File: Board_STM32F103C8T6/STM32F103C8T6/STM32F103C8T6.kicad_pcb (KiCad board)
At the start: 4 copper layers, 96 x 96 mm, 113 parts, among them J301 BOOT, J401 BATTERY, J402 I2C, J403 H2O, J404 USB_B_Micro, J405 SWD, J406 USART1, J407 CIRCUIT_SENSOR, J408 BLUETOOTH, J409 RPM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

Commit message: updated layout
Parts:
- C702: value 250n -> 220n
- R703: value 4,7K -> 4k7
- U201: value LD1117S33TR_SOT223 -> LD1117S33TR

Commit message: Changed Crystals
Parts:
- C201, C302, C303, C304, C305, C308, C401, C502, C503, C504, C602, C802, C803, C804: value 100n -> 0.1uF
- C202, C501, C601, C701, C703, C801: value 10u -> 10uF
- C301: value 4u7 -> 4.7uF
- C306: value 1u -> 1uF
- C307, C805: value 10n -> 0.01uF
- C309, C311: value 12p -> 24pF
- C310, C312: value 6.8p -> 13pF
- C402, C403: value 47p -> 47pF
- C505: value 2n2 -> 2200pF
- C702: value 220n -> 0.1uF
- L301: value 39n -> 39nH
- L801: value 100n -> 100nH
- R201, R311, R319, R603: value 1k5 -> 1.5kΩ
- R301, R302: value 2k2 -> 2.2kΩ
- R303, R304, R306, R308, R309, R310, R313, R314: value 100k -> 100kΩ
- R305: value 1k5 -> 787Ω
- R307: value 7.5k -> 36kΩ
- R312, R705: value 100 -> 100kΩ
- R315, R316, R318, R320: value 10k -> 10kΩ
- R317: value 4k7 -> 4.7kΩ
- R401, R402: value 22 -> 22kΩ
- R601, R602: value 1k -> 1kΩ
- R701, R702, R704, R706: value 10K -> 10kΩ
- R703: value 4k7 -> 10kΩ
- R801, R802: value 0 -> 0kΩ
- R803: value 10 -> 10kΩ
- Y301: value 8Mhz -> 8MHz; footprint Crystal:Crystal_SMD_5032-2Pin_5.0x3.2mm_HandSoldering -> Crystal:Crystal_SMD_HC49-SD_HandSoldering
- Y302: value 32.768KHZ -> 32.768KHz; footprint Crystal:Crystal_SMD_3215-2Pin_3.2x1.5mm -> Crystal:Crystal_SMD_Abracon_ABS25-4Pin_8.0x3.8mm
- moved Y301 4.27 mm to (108.5, 80.0)
- moved C310 4.19 mm to (113.0, 57.0), turned to 90 degrees
- moved R706 3.76 mm to (124.0, 87.0), turned to 90 degrees
- moved C309 3.10 mm to (113.0, 71.0), turned to 90 degrees
- moved C311 2.97 mm to (113.0, 82.5), turned to 270 degrees
- moved Y302 2.69 mm to (108.5, 61.0), turned to 0 degrees
- moved R307 1.80 mm to (113.0, 66.5)
- turned C312 to 180 degrees
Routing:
- net LSE_IN: track 19.3 -> 27.6 mm
- net USART2_RX: track 94.2 -> 102.4 mm
- net USART2_TX: track 97.1 -> 104.5 mm
- net GND: track 63.2 -> 69.8 mm, vias 84 -> 88
- net +5V: track 72.3 -> 65.9 mm
- net LED_STATUS: track 35.6 -> 41.7 mm
- net +3V3: track 152.2 -> 147.1 mm, vias 40 -> 41
- net H2O_NTC+: track 54.9 -> 49.9 mm, vias 1 -> 0
- net Net-(C312-Pad1): track 4.89 -> 7.95 mm
- net Net-(C311-Pad1): track 11.8 -> 9.49 mm
- net BOOT0: track 67.4 -> 69.6 mm
- net LSE_OUT: track 12.4 -> 10.8 mm
- net RPM_SENSOR: track 16.1 -> 15.0 mm
- net HSE_IN: track 14.2 -> 13.4 mm

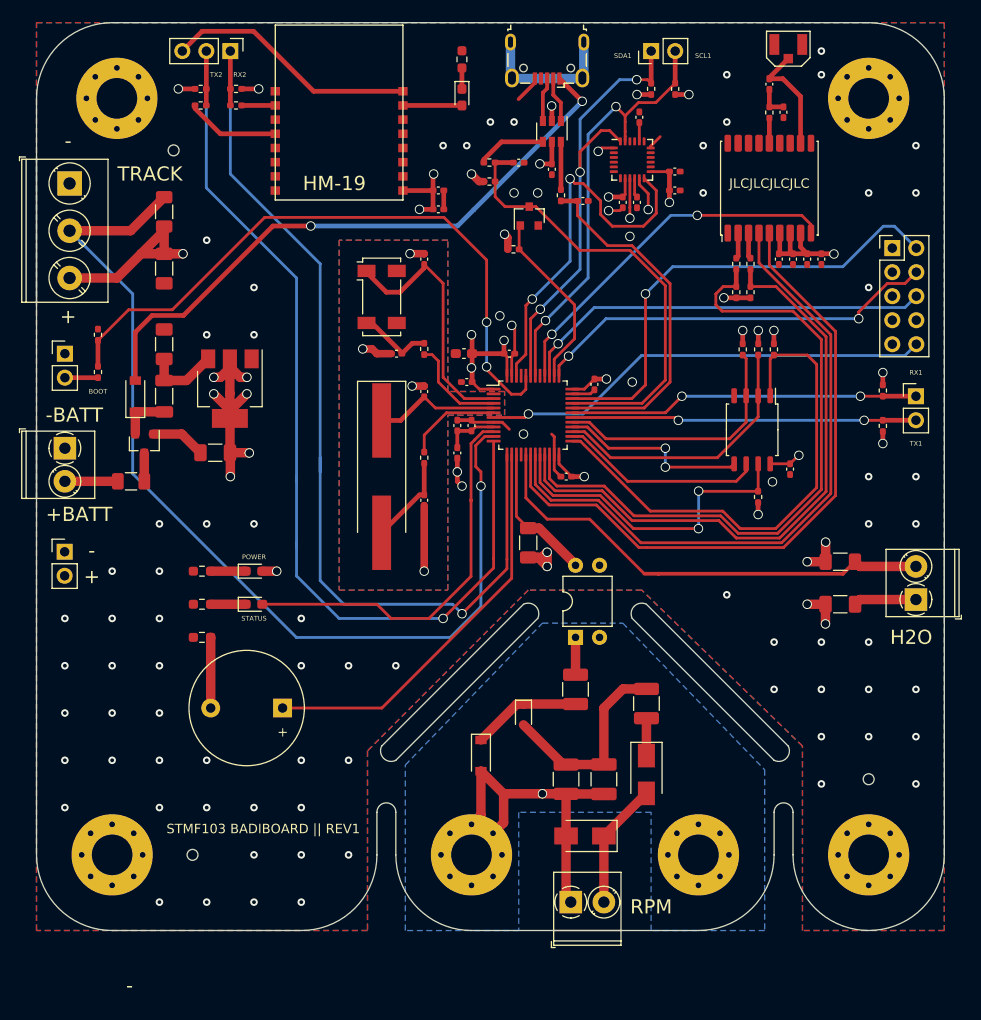
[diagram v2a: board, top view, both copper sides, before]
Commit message: Change part number
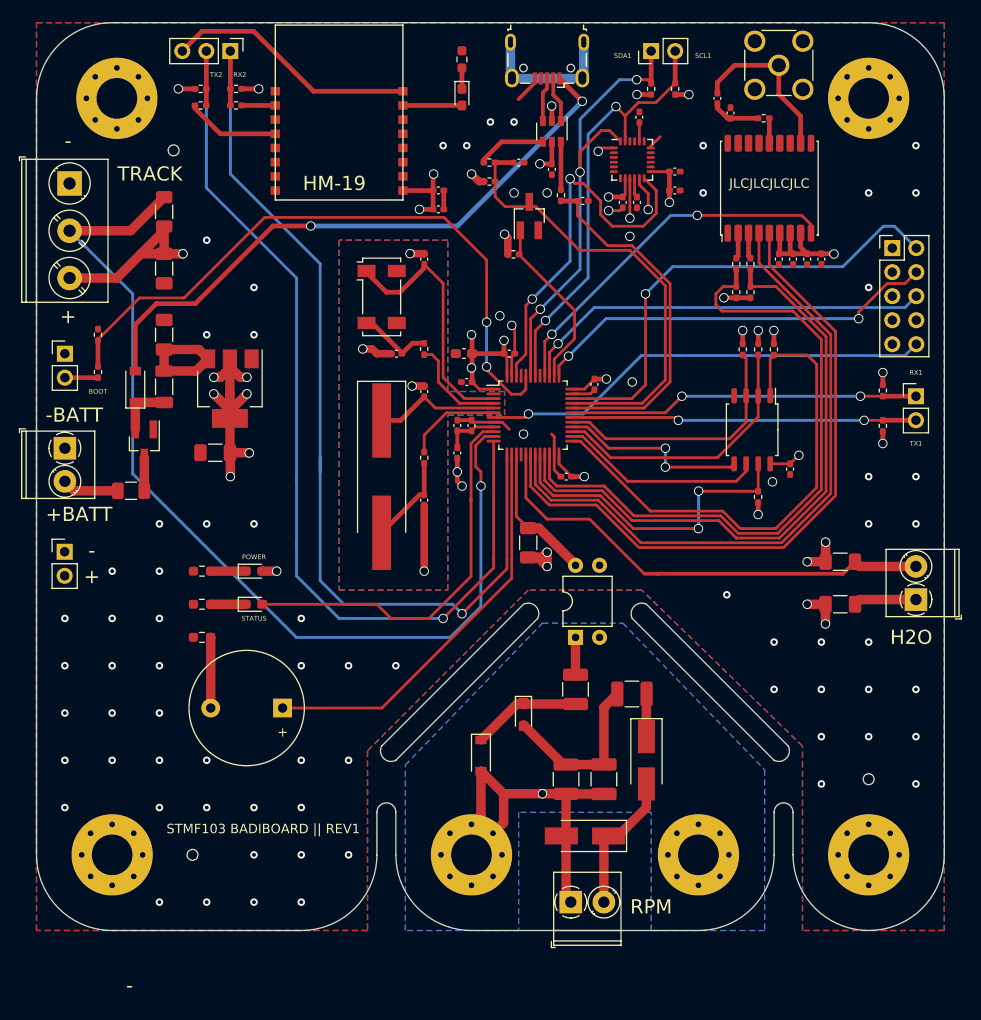
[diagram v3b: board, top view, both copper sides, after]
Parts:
- D701, D702: footprint Diode_SMD:D_SMA -> Diode_SMD:D_SMA_Handsoldering
- D703: footprint Diode_SMD:D_SOD-323F -> Diode_SMD:D_SOD-323_HandSoldering
- J801: footprint MyFootprints:BWIPX-1-001E -> Connector_Coaxial:SMA_Molex_73251-2200_Horizontal
- Q201: value AO3401A -> SI2301CDS-T1-BE3; footprint Package_TO_SOT_SMD:SOT-23 -> Package_TO_SOT_SMD:SOT-23_Handsoldering
- Q301: value BSS123 -> SI2312BDS-T1-BE3; footprint Package_TO_SOT_SMD:SOT-23 -> Package_TO_SOT_SMD:SOT-23_Handsoldering
- moved L801 5.70 mm to (144.0, 40.0)
- moved C805 5.60 mm to (145.4, 41.5), turned to 90 degrees
- moved J801 2.42 mm to (150.5, 36.5), turned to 0 degrees
- moved R703 1.83 mm to (135.0, 103.0), turned to 0 degrees
- moved D702 1.50 mm to (136.5, 110.0)
- moved C201 1.00 mm to (85.5, 65.0)
- moved D201 1.00 mm to (82.5, 70.5)
- moved F201 1.00 mm to (82.0, 81.5)
- moved FB201 1.00 mm to (85.5, 70.5)
- moved R803 0.86 mm to (148.9, 42.1), turned to 0 degrees
- moved R320 0.53 mm to (122.4, 56.5)
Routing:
- net GND: track 69.8 -> 63.9 mm, vias 88 -> 84
- net Net-(J801-Pad1): track 12.0 -> 17.6 mm
- net Net-(C201-Pad1): track 7.87 -> 12.5 mm
- net Net-(C702-Pad1): track 21.5 -> 18.3 mm
- net Net-(C805-Pad1): track 3.32 -> 5.22 mm
- net COIL_RPM: track 13.4 -> 14.7 mm
- net Net-(D702-Pad1): track 3.95 -> 4.52 mm
- net +5V: track 65.9 -> 65.4 mm
- net +3V3: track 147.1 -> 147.6 mm
- net Net-(F201-Pad1): track 3.00 -> 3.50 mm
- net Net-(D201-Pad1): track 5.41 -> 5.91 mm

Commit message: Added descriptions
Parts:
- added R403: 5.1kΩ, Resistor_SMD:R_0402_1005Metric_Pad0.72x0.64mm_HandSolder, F.Cu at (123.0, 42.5)
- added R404: 5.1kΩ, Resistor_SMD:R_0402_1005Metric_Pad0.72x0.64mm_HandSolder, F.Cu at (130.0, 42.5)
- J404: value USB_B_Micro -> USB_C_Receptacle_USB2.0; footprint Connector_USB:USB_Micro-B_Wuerth_629105150521 -> Connector_USB:USB_C_Receptacle_Palconn_UTC16-G
- R705: value 100kΩ -> 100Ω
- moved J404 0.71 mm to (126.5, 36.5)
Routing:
- net Net-(J404-PadS1): track 0.00 -> 17.0 mm
- net Net-(J404-Pad6): track 15.2 -> 0.00 mm
- net +5V: track 65.4 -> 74.5 mm, vias 2 -> 3
- net GND: track 63.9 -> 70.2 mm, vias 84 -> 83
- net Net-(J404-PadA5): track 0.00 -> 4.17 mm
- net Net-(J404-PadB5): track 0.00 -> 3.97 mm
- net USB_CONN_D-: track 4.83 -> 6.20 mm
- net USB_CONN_D+: track 4.69 -> 5.51 mm
